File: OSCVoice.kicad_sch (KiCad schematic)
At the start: 39 parts, among them U15 4066, U16 TL072, U22 SSI2131, U5 MCP6004, U8 4066

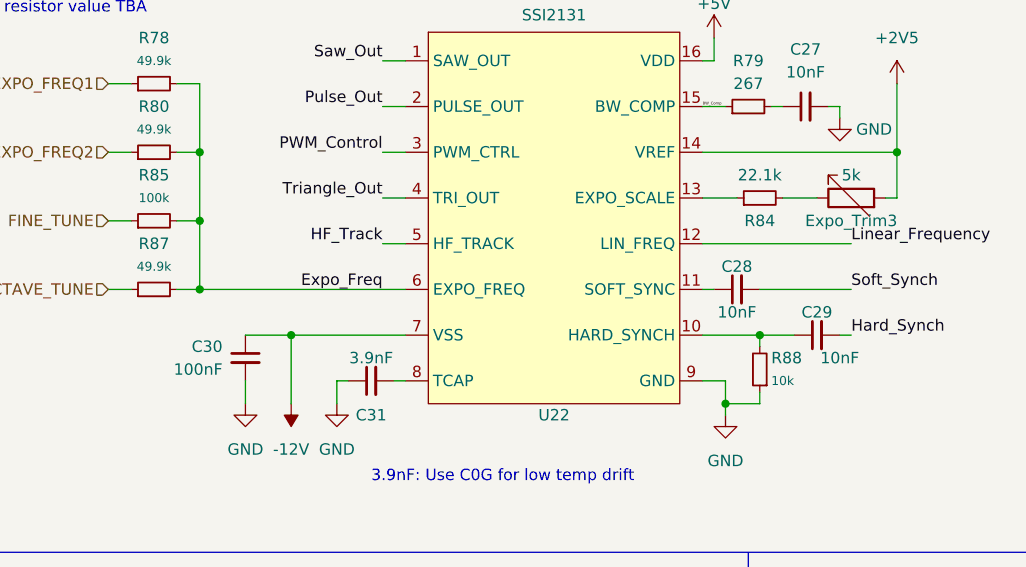
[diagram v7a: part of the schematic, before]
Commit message: Fixed ground connections on component board
Added JLC PCB plug-in
Schematic clean-up
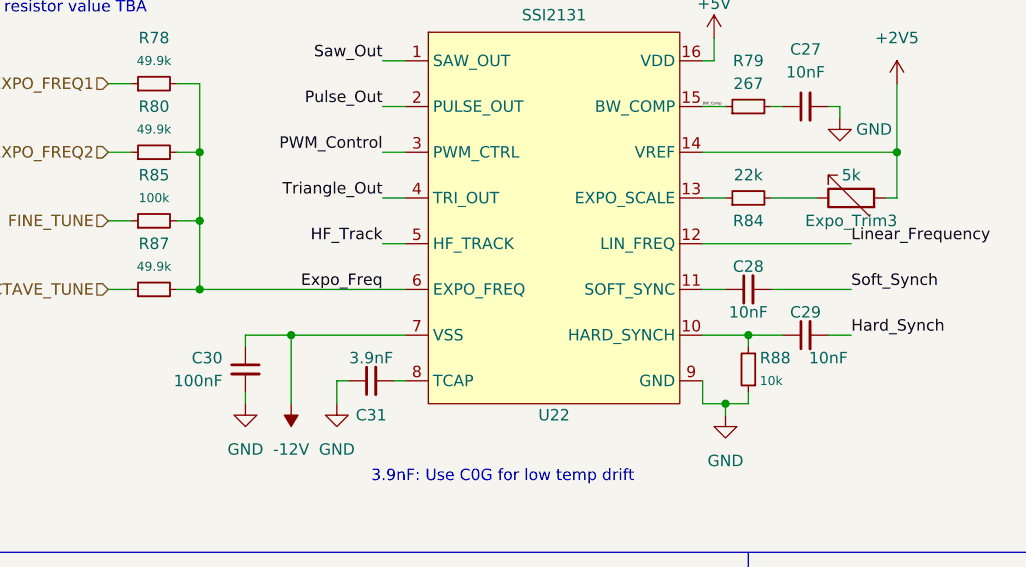
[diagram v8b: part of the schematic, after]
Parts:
- R84: value 22.1k -> 22k
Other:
- moved on the sheet: C28, C29, C30, R84, R88
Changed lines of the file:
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@@
   (title_block
     (title "Quadraphone Voice")
+    (date "2023-01-27")
+    (rev "v1.0")
     (company "Mountjoy Modular")
   )
@@
   (junction (at 118.11 63.5) (diameter 0) (color 0 0 0 0)
   )
-  (junction (at 121.92 55.88) (diameter 0) (color 0 0 0 0)
-  )
   (junction (at 110.49 139.7) (diameter 0) (color 0 0 0 0)
   )
@@
   (junction (at 125.73 157.48) (diameter 0) (color 0 0 0 0)
   )
+  (junction (at 120.65 55.88) (diameter 0) (color 0 0 0 0)
+  )
   (junction (at 59.69 43.18) (diameter 0) (color 0 0 0 0)
   )
@@
     (stroke (width 0) (type default) (color 0 0 0 0))
   )
-  (wire (pts (xy 115.57 40.64) (xy 119.38 40.64))
+  (wire (pts (xy 115.57 40.64) (xy 118.11 40.64))
     (stroke (width 0) (type default) (color 0 0 0 0))
   )
@@
     (stroke (width 0) (type default) (color 0 0 0 0))
   )
+  (wire (pts (xy 115.57 63.5) (xy 118.11 63.5))
+    (stroke (width 0) (type default) (color 0 0 0 0))
+  )
   (wire (pts (xy 97.79 139.7) (xy 101.6 139.7))
     (stroke (width 0) (type default) (color 0 0 0 0))
@@
     (stroke (width 0) (type default) (color 0 0 0 0))
   )
-  (wire (pts (xy 121.92 50.8) (xy 132.08 50.8))
+  (wire (pts (xy 123.19 50.8) (xy 132.08 50.8))
     (stroke (width 0) (type default) (color 0 0 0 0))
   )
@@
     (stroke (width 0) (type default) (color 0 0 0 0))
   )
-  (wire (pts (xy 118.11 60.96) (xy 118.11 63.5))
+  (wire (pts (xy 115.57 60.96) (xy 115.57 63.5))
     (stroke (width 0) (type default) (color 0 0 0 0))
   )
@@
     (stroke (width 0) (type default) (color 0 0 0 0))
   )
-  (wire (pts (xy 130.81 55.88) (xy 132.08 55.88))
+  (wire (pts (xy 129.54 55.88) (xy 132.08 55.88))
     (stroke (width 0) (type default) (color 0 0 0 0))
   )
@@
     (stroke (width 0) (type default) (color 0 0 0 0))
   )
+  (wire (pts (xy 64.77 55.88) (xy 64.77 57.15))
+    (stroke (width 0) (type default) (color 0 0 0 0))
+  )
   (wire (pts (xy 247.65 31.75) (xy 251.46 31.75))
     (stroke (width 0) (type default) (color 0 0 0 0))
@@
     (stroke (width 0) (type default) (color 0 0 0 0))
   )
-  (wire (pts (xy 115.57 60.96) (xy 118.11 60.96))
-    (stroke (width 0) (type default) (color 0 0 0 0))
-  )
   (wire (pts (xy 49.53 35.56) (xy 52.07 35.56))
     (stroke (width 0) (type default) (color 0 0 0 0))
@@
     (stroke (width 0) (type default) (color 0 0 0 0))
   )
-  (wire (pts (xy 124.46 40.64) (xy 128.27 40.64))
+  (wire (pts (xy 123.19 40.64) (xy 128.27 40.64))
     (stroke (width 0) (type default) (color 0 0 0 0))
   )
@@
     (stroke (width 0) (type default) (color 0 0 0 0))
   )
-  (wire (pts (xy 115.57 50.8) (xy 116.84 50.8))
-    (stroke (width 0) (type default) (color 0 0 0 0))
-  )
-  (wire (pts (xy 64.77 60.96) (xy 64.77 63.5))
+  (wire (pts (xy 115.57 50.8) (xy 118.11 50.8))
     (stroke (width 0) (type default) (color 0 0 0 0))
   )
@@
     (stroke (width 0) (type default) (color 0 0 0 0))
   )
-  (wire (pts (xy 121.92 55.88) (xy 121.92 57.15))
+  (wire (pts (xy 120.65 55.88) (xy 120.65 57.15))
     (stroke (width 0) (type default) (color 0 0 0 0))
   )
@@
     (stroke (width 0) (type default) (color 0 0 0 0))
   )
+  (wire (pts (xy 64.77 62.23) (xy 64.77 63.5))
+    (stroke (width 0) (type default) (color 0 0 0 0))
+  )
   (wire (pts (xy 64.77 55.88) (xy 69.85 55.88))
     (stroke (width 0) (type default) (color 0 0 0 0))
@@
     (stroke (width 0) (type default) (color 0 0 0 0))
   )
-  (wire (pts (xy 115.57 55.88) (xy 121.92 55.88))
+  (wire (pts (xy 115.57 55.88) (xy 120.65 55.88))
     (stroke (width 0) (type default) (color 0 0 0 0))
   )
@@
     (stroke (width 0) (type default) (color 0 0 0 0))
   )
-  (wire (pts (xy 121.92 55.88) (xy 125.73 55.88))
-    (stroke (width 0) (type default) (color 0 0 0 0))
-  )
   (wire (pts (xy 69.85 55.88) (xy 82.55 55.88))
     (stroke (width 0) (type default) (color 0 0 0 0))
@@
     (stroke (width 0) (type default) (color 0 0 0 0))
   )
-  (wire (pts (xy 121.92 62.23) (xy 121.92 63.5))
+  (wire (pts (xy 120.65 62.23) (xy 120.65 63.5))
     (stroke (width 0) (type default) (color 0 0 0 0))
   )
@@
     (stroke (width 0) (type default) (color 0 0 0 0))
   )
-  (wire (pts (xy 121.92 63.5) (xy 118.11 63.5))
+  (wire (pts (xy 120.65 55.88) (xy 124.46 55.88))
+    (stroke (width 0) (type default) (color 0 0 0 0))
+  )
+  (wire (pts (xy 120.65 63.5) (xy 118.11 63.5))
     (stroke (width 0) (type default) (color 0 0 0 0))
   )
@@
     (pin "1")
   )
-  (symbol (lib_id "Device:C_Small") (at 128.27 55.88 90) (unit 1)
-    (in_bom yes) (on_board yes)
-    (property "Reference" "C29" (id 0) (at 128.27 53.34 90))
-    (property "Value" "10nF" (id 1) (at 130.81 58.42 90))
-    (property "Footprint" "Capacitor_SMD:C_0603_1608Metric_Pad1.08x0.95mm_HandSolder" (id 2) (at 128.27 55.88 0)
-      (effects (font (size 1.27 1.27)) hide)
-    )
-    (property "Datasheet" "~" (id 3) (at 128.27 55.88 0)
+  (symbol (lib_id "Device:C_Small") (at 127 55.88 90) (unit 1)
+    (in_bom yes) (on_board yes)
+    (property "Reference" "C29" (id 0) (at 127 53.34 90))
+    (property "Value" "10nF" (id 1) (at 129.54 58.42 90))
+    (property "Footprint" "Capacitor_SMD:C_0603_1608Metric_Pad1.08x0.95mm_HandSolder" (id 2) (at 127 55.88 0)
+      (effects (font (size 1.27 1.27)) hide)
+    )
+    (property "Datasheet" "~" (id 3) (at 127 55.88 0)
       (effects (font (size 1.27 1.27)) hide)
     )
@@
     (pin "2")
   )
-  (symbol (lib_id "Device:R_Small") (at 121.92 40.64 90) (unit 1)
-    (in_bom yes) (on_board yes)
-    (property "Reference" "R84" (id 0) (at 121.92 43.18 90))
-    (property "Value" "22.1k" (id 1) (at 121.92 38.1 90))
-    (property "Footprint" "Resistor_SMD:R_0603_1608Metric" (id 2) (at 121.92 40.64 0)
-      (effects (font (size 1.27 1.27)) hide)
-    )
-    (property "Datasheet" "~" (id 3) (at 121.92 40.64 0)
+  (symbol (lib_id "Device:R_Small") (at 120.65 40.64 90) (unit 1)
+    (in_bom yes) (on_board yes)
+    (property "Reference" "R84" (id 0) (at 120.65 43.18 90))
+    (property "Value" "22k" (id 1) (at 120.65 38.1 90))
+    (property "Footprint" "Resistor_SMD:R_0603_1608Metric" (id 2) (at 120.65 40.64 0)
+      (effects (font (size 1.27 1.27)) hide)
+    )
+    (property "Datasheet" "~" (id 3) (at 120.65 40.64 0)
       (effects (font (size 1.27 1.27)) hide)
     )
@@
     (pin "3")
   )
-  (symbol (lib_id "Device:C_Small") (at 119.38 50.8 90) (unit 1)
-    (in_bom yes) (on_board yes)
-    (property "Reference" "C28" (id 0) (at 119.38 48.26 90))
-    (property "Value" "10nF" (id 1) (at 119.38 53.34 90))
-    (property "Footprint" "Capacitor_SMD:C_0603_1608Metric_Pad1.08x0.95mm_HandSolder" (id 2) (at 119.38 50.8 0)
-      (effects (font (size 1.27 1.27)) hide)
-    )
-    (property "Datasheet" "~" (id 3) (at 119.38 50.8 0)
+  (symbol (lib_id "Device:C_Small") (at 120.65 50.8 90) (unit 1)
+    (in_bom yes) (on_board yes)
+    (property "Reference" "C28" (id 0) (at 120.65 48.26 90))
+    (property "Value" "10nF" (id 1) (at 120.65 53.34 90))
+    (property "Footprint" "Capacitor_SMD:C_0603_1608Metric_Pad1.08x0.95mm_HandSolder" (id 2) (at 120.65 50.8 0)
+      (effects (font (size 1.27 1.27)) hide)
+    )
+    (property "Datasheet" "~" (id 3) (at 120.65 50.8 0)
       (effects (font (size 1.27 1.27)) hide)
     )
@@
     (pin "8")
   )
-  (symbol (lib_id "Device:R_Small") (at 121.92 59.69 180) (unit 1)
-    (in_bom yes) (on_board yes)
-    (property "Reference" "R88" (id 0) (at 123.19 58.42 0)
+  (symbol (lib_id "Device:R_Small") (at 120.65 59.69 180) (unit 1)
+    (in_bom yes) (on_board yes)
+    (property "Reference" "R88" (id 0) (at 121.92 58.42 0)
       (effects (font (size 1.27 1.27)) (justify right))
     )
-    (property "Value" "10k" (id 1) (at 123.19 60.96 0)
+    (property "Value" "10k" (id 1) (at 121.92 60.96 0)
       (effects (font (size 1 1)) (justify right))
     )
-    (property "Footprint" "Resistor_SMD:R_0603_1608Metric" (id 2) (at 121.92 59.69 0)
-      (effects (font (size 1.27 1.27)) hide)
-    )
-    (property "Datasheet" "~" (id 3) (at 121.92 59.69 0)
+    (property "Footprint" "Resistor_SMD:R_0603_1608Metric" (id 2) (at 120.65 59.69 0)
+      (effects (font (size 1.27 1.27)) hide)
+    )
+    (property "Datasheet" "~" (id 3) (at 120.65 59.69 0)
       (effects (font (size 1.27 1.27)) hide)
     )
@@
     (pin "1")
   )
-  (symbol (lib_id "Device:C_Small") (at 64.77 58.42 0) (unit 1)
-    (in_bom yes) (on_board yes) (fields_autoplaced)
-    (property "Reference" "C30" (id 0) (at 62.23 57.1562 0)
+  (symbol (lib_id "Device:C_Small") (at 64.77 59.69 0) (unit 1)
+    (in_bom yes) (on_board yes) (fields_autoplaced)
+    (property "Reference" "C30" (id 0) (at 62.23 58.4262 0)
       (effects (font (size 1.27 1.27)) (justify right))
     )
-    (property "Value" "100nF" (id 1) (at 62.23 59.6962 0)
+    (property "Value" "100nF" (id 1) (at 62.23 60.9662 0)
       (effects (font (size 1.27 1.27)) (justify right))
     )
-    (property "Footprint" "Capacitor_SMD:C_0603_1608Metric_Pad1.08x0.95mm_HandSolder" (id 2) (at 64.77 58.42 0)
-      (effects (font (size 1.27 1.27)) hide)
-    )
-    (property "Datasheet" "~" (id 3) (at 64.77 58.42 0)
-      (effects (font (size 1.27 1.27)) hide)
-    )
+    (property "Footprint" "Capacitor_SMD:C_0603_1608Metric_Pad1.08x0.95mm_HandSolder" (id 2) (at 64.77 59.69 0)
+      (effects (font (size 1.27 1.27)) hide)
+    )
+    (property "Datasheet" "~" (id 3) (at 64.77 59.69 0)
+      (effects (font (size 1.27 1.27)) hide)
+    )
